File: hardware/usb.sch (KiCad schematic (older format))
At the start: 33 parts, among them U31 USB-MICRO, U32 93LC46B, U33 FT2232H, Y1 ABM10-167-12.000MHZ-T3

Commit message: Current working version.
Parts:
- removed U31: USB-MICRO, fmcw3:USB_MICRO, symbol USB-MICRO
- removed U32: 93LC46B, fmcw3:SOT-23-6, symbol 93LC46B
- removed U33: FT2232H, Housings_QFP:LQFP-64_10x10mm_Pitch0.5mm, symbol FT2232H
- added J2: USB_B_Micro, fmcw3:USB_MICRO, symbol Connector:USB_B_Micro
- added U14: FT2232H, Package_QFP:LQFP-64_10x10mm_P0.5mm, symbol Interface_USB:FT2232H
- added U31: 93LCxxB, Package_TO_SOT_SMD:SOT-23-6, symbol Memory_EEPROM:93LCxxB
- C152, C153, C154, C158, C159, C160, C161, C207, C208, C209, C210, C211, C212: footprint fmcw3:C_0402b -> Capacitor_SMD:C_0402_1005Metric; symbol C -> Device:C
- C155, C156, C157: footprint fmcw3:C_0603b -> Capacitor_SMD:C_0603_1608Metric; symbol C -> Device:C
- FB12, FB14: symbol FILTER -> Device:Ferrite_Bead
- R71, R72, R73, R79, R80, R81, R82, R83, R84, R85, R88: symbol R -> Device:R
- Y1: footprint fmcw3:ABM10 -> Crystal:Crystal_SMD_Abracon_ABM10-4Pin_2.5x2.0mm; symbol XTAL_SMD4 -> Device:Crystal
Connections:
- wire segments 108 -> 129

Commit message: Dropped the 3 from the end of the project name.
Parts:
- FB12, FB14: footprint fmcw3:C_0603b -> fmcw:C_0603b
- J2: footprint fmcw3:USB_MICRO -> fmcw:USB_MICRO
- R71, R72, R73, R79, R80, R81, R82, R83, R84, R85, R88: footprint fmcw3:R_0402b -> fmcw:R_0402b
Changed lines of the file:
@@
 EESchema Schematic File Version 4
-LIBS:fmcw3-cache
+LIBS:fmcw-cache
 EELAYER 26 0
 EELAYER END
@@
 F 0 "R80" V 4300 3350 50  0000 C CNN
 F 1 "0" V 4400 3350 50  0000 C CNN
-F 2 "fmcw3:R_0402b" V 4330 3350 30  0001 C CNN
+F 2 "fmcw:R_0402b" V 4330 3350 30  0001 C CNN
 F 3 "" H 4400 3350 30  0000 C CNN
 	1    4400 3350
@@
 F 0 "R81" V 4480 3450 50  0000 C CNN
 F 1 "0" V 4400 3450 50  0000 C CNN
-F 2 "fmcw3:R_0402b" V 4330 3450 30  0001 C CNN
+F 2 "fmcw:R_0402b" V 4330 3450 30  0001 C CNN
 F 3 "" H 4400 3450 30  0000 C CNN
 	1    4400 3450
@@
 F 0 "R84" V 8080 4150 50  0000 C CNN
 F 1 "33" V 8000 4150 50  0000 C CNN
-F 2 "fmcw3:R_0402b" V 7930 4150 30  0001 C CNN
+F 2 "fmcw:R_0402b" V 7930 4150 30  0001 C CNN
 F 3 "" H 8000 4150 30  0000 C CNN
 	1    8000 4150
@@
 F 0 "R88" V 8480 4250 50  0000 C CNN
 F 1 "33" V 8400 4250 50  0000 C CNN
-F 2 "fmcw3:R_0402b" V 8330 4250 30  0001 C CNN
+F 2 "fmcw:R_0402b" V 8330 4250 30  0001 C CNN
 F 3 "" H 8400 4250 30  0000 C CNN
 	1    8400 4250
@@
 F 0 "R85" V 8080 4450 50  0000 C CNN
 F 1 "33" V 8000 4450 50  0000 C CNN
-F 2 "fmcw3:R_0402b" V 7930 4450 30  0001 C CNN
+F 2 "fmcw:R_0402b" V 7930 4450 30  0001 C CNN
 F 3 "" H 8000 4450 30  0000 C CNN
 	1    8000 4450
@@
 F 0 "R73" V 1380 4200 50  0000 C CNN
 F 1 "10k" V 1300 4200 50  0000 C CNN
-F 2 "fmcw3:R_0402b" V 1230 4200 30  0001 C CNN
+F 2 "fmcw:R_0402b" V 1230 4200 30  0001 C CNN
 F 3 "" H 1300 4200 30  0000 C CNN
 	1    1300 4200
@@
 F 0 "R79" V 1380 4600 50  0000 C CNN
 F 1 "2.2k" V 1300 4600 50  0000 C CNN
-F 2 "fmcw3:R_0402b" V 1230 4600 30  0001 C CNN
+F 2 "fmcw:R_0402b" V 1230 4600 30  0001 C CNN
 F 3 "" H 1300 4600 30  0000 C CNN
 	1    1300 4600
@@
 F 0 "FB12" V 4500 1500 50  0000 C CNN
 F 1 "BLM18PG181SN1D" V 4400 1300 50  0000 C CNN
-F 2 "fmcw3:C_0603b" H 4550 1300 60  0001 C CNN
+F 2 "fmcw:C_0603b" H 4550 1300 60  0001 C CNN
 F 3 "" H 4550 1300 60  0000 C CNN
 	1    4550 1300
@@
 F 0 "FB14" V 4500 900 50  0000 C CNN
 F 1 "BLM18PG181SN1D" V 4400 1050 50  0000 C CNN
-F 2 "fmcw3:C_0603b" H 4550 1050 60  0001 C CNN
+F 2 "fmcw:C_0603b" H 4550 1050 60  0001 C CNN
 F 3 "" H 4550 1050 60  0000 C CNN
 	1    4550 1050
@@
 F 0 "R72" V 4930 3850 50  0000 C CNN
 F 1 "1k" V 4850 3850 50  0000 C CNN
-F 2 "fmcw3:R_0402b" V 4780 3850 30  0001 C CNN
+F 2 "fmcw:R_0402b" V 4780 3850 30  0001 C CNN
 F 3 "" H 4850 3850 30  0000 C CNN
 	1    4850 3850
@@
 F 0 "R71" V 4330 3900 50  0000 C CNN
 F 1 "12k" V 4250 3900 50  0000 C CNN
-F 2 "fmcw3:R_0402b" V 4180 3900 30  0001 C CNN
+F 2 "fmcw:R_0402b" V 4180 3900 30  0001 C CNN
 F 3 "" H 4250 3900 30  0000 C CNN
 	1    4250 3900
@@
 F 0 "R82" V 8680 5600 50  0000 C CNN
 F 1 "4.7k" V 8600 5600 50  0000 C CNN
-F 2 "fmcw3:R_0402b" V 8530 5600 30  0001 C CNN
+F 2 "fmcw:R_0402b" V 8530 5600 30  0001 C CNN
 F 3 "" H 8600 5600 30  0000 C CNN
 	1    8600 5600
@@
 F 0 "R83" V 8680 5950 50  0000 C CNN
 F 1 "10k" V 8600 5950 50  0000 C CNN
-F 2 "fmcw3:R_0402b" V 8530 5950 30  0001 C CNN
+F 2 "fmcw:R_0402b" V 8530 5950 30  0001 C CNN
 F 3 "" H 8600 5950 30  0000 C CNN
 	1    8600 5950
@@
 F 0 "J2" H 1305 3417 50  0000 C CNN
 F 1 "USB_B_Micro" H 1305 3326 50  0000 C CNN
-F 2 "fmcw3:USB_MICRO" H 1400 2900 50  0001 C CNN
+F 2 "fmcw:USB_MICRO" H 1400 2900 50  0001 C CNN
 F 3 "~" H 1400 2900 50  0001 C CNN
 	1    1250 2950

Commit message: Modularized LaTeX documentation.
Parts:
- J2: footprint fmcw:USB_MICRO -> Connector_USB:USB_Micro-B_Amphenol_10103594-0001LF_Horizontal
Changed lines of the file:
@@
 EESchema Schematic File Version 4
 LIBS:fmcw-cache
-EELAYER 26 0
+EELAYER 29 0
 EELAYER END
 $Descr A4 11693 8268
@@
 F 0 "J2" H 1305 3417 50  0000 C CNN
 F 1 "USB_B_Micro" H 1305 3326 50  0000 C CNN
-F 2 "fmcw:USB_MICRO" H 1400 2900 50  0001 C CNN
+F 2 "Connector_USB:USB_Micro-B_Amphenol_10103594-0001LF_Horizontal" H 1400 2900 50  0001 C CNN
 F 3 "~" H 1400 2900 50  0001 C CNN
 	1    1250 2950

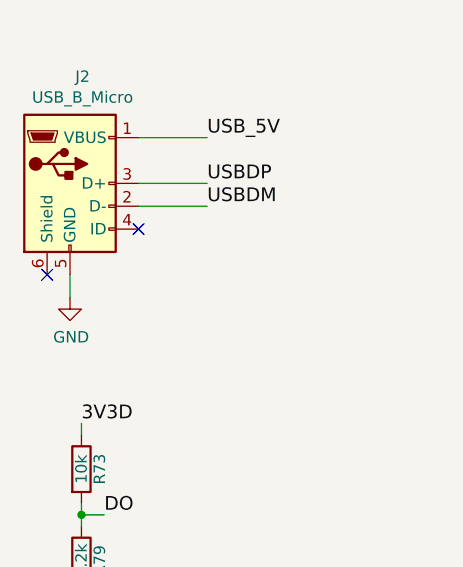
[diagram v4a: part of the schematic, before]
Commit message: Documentation for TPS5420D buck converter.
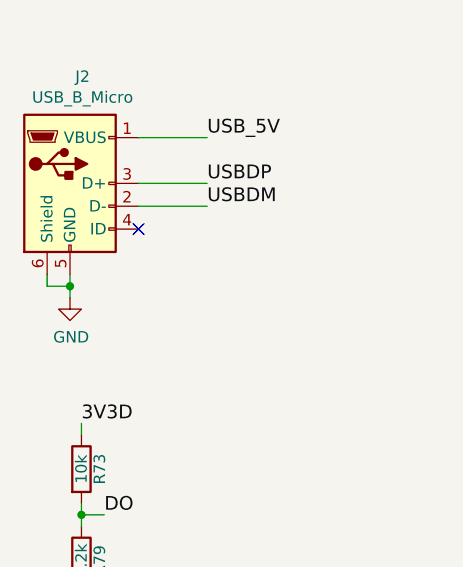
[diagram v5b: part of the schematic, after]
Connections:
- net GND: now also J2.6 (Shield)
- no-connect marks 17 -> 16
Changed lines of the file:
@@
 USBDM
 NoConn ~ 1550 3150
-NoConn ~ 1150 3350
 Wire Wire Line
-	1250 3350 1250 3450
+	1250 3350 1250 3400
 $Comp
 L power:GND #PWR0255
@@
 Wire Wire Line
 	8600 5350 8600 5450
+Wire Wire Line
+	1150 3350 1150 3400
+Wire Wire Line
+	1150 3400 1250 3400
+Connection ~ 1250 3400
+Wire Wire Line
+	1250 3400 1250 3450
 $EndSCHEMATC

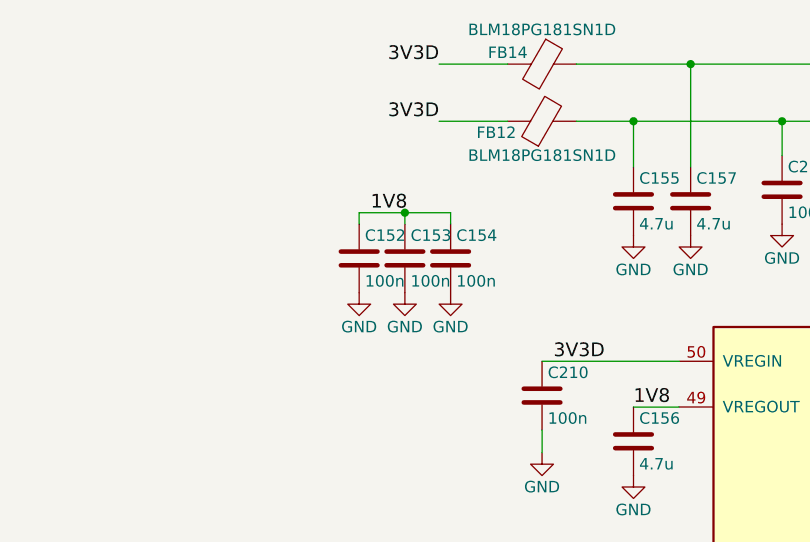
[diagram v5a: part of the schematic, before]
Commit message: Improved top level documentation.
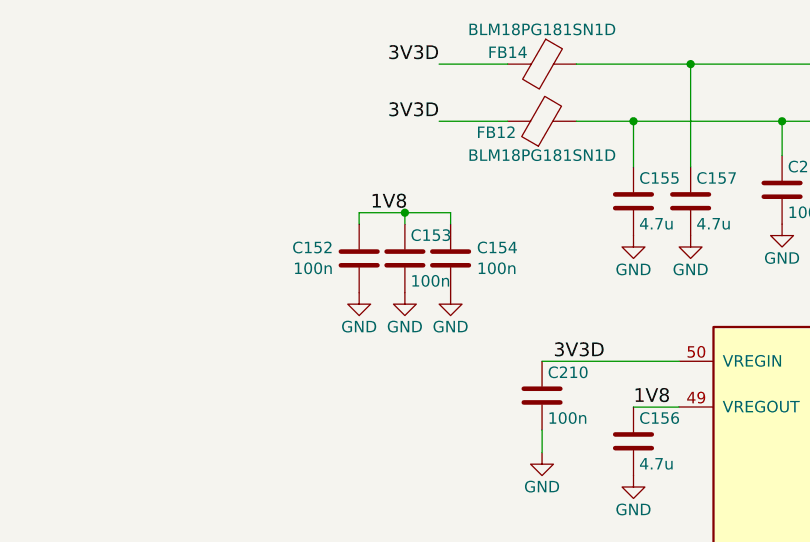
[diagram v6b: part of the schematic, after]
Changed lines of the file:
@@
 U 1 1 596C4A23
 P 3750 1900
-F 0 "C152" H 3775 2000 50  0000 L CNN
-F 1 "100n" H 3775 1800 50  0000 L CNN
+F 0 "C152" H 3636 1946 50  0000 R CNN
+F 1 "100n" H 3636 1855 50  0000 R CNN
 F 2 "Capacitor_SMD:C_0402_1005Metric" H 3788 1750 30  0001 C CNN
 F 3 "" H 3750 1900 60  0000 C CNN
@@
 U 1 1 596C4AFE
 P 4150 1900
-F 0 "C154" H 4175 2000 50  0000 L CNN
-F 1 "100n" H 4175 1800 50  0000 L CNN
+F 0 "C154" H 4265 1946 50  0000 L CNN
+F 1 "100n" H 4265 1855 50  0000 L CNN
 F 2 "Capacitor_SMD:C_0402_1005Metric" H 4188 1750 30  0001 C CNN
 F 3 "" H 4150 1900 60  0000 C CNN
